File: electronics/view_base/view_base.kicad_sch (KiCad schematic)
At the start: 258 parts, among them J1 USB_C_Receptacle_USB2.0, J2 A, J3 B, J4 LCD, J5 59453-081110EDHLF, J6 BLDC, J7 SM04B-SRSS-TB(LF)(SN), J8 SM04B-SRSS-TB(LF)(SN), J9 SM04B-SRSS-TB(LF)(SN), Q1 MMBT4403, Q2 BSS138, Q3 BSS138, SW1 RST, SW2 Boot, U1 SN74LV1T34DBV, U10 LP5907MFX-2.8, U11 ESP32-S3-WROOM-1U-N16R8, U2 MT6701-CT, U3 VEML7700, U4 AMS1117-3.3, U5 USBLC6-2SC6, U6 HX711, U8 TMC6300, U9 VL53L0CXV0DH_1

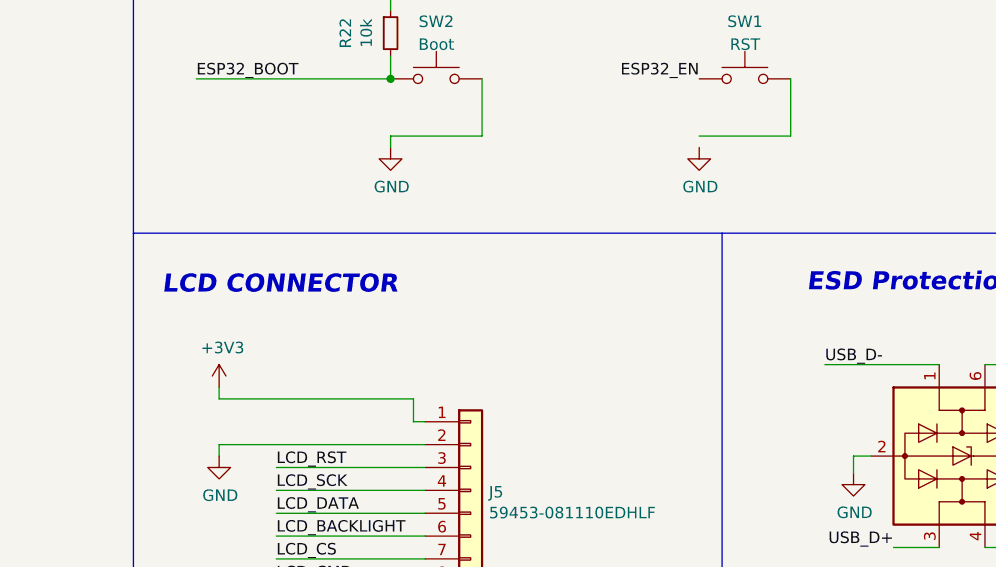
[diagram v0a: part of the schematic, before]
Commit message: Check github action for detect diff in the sch file
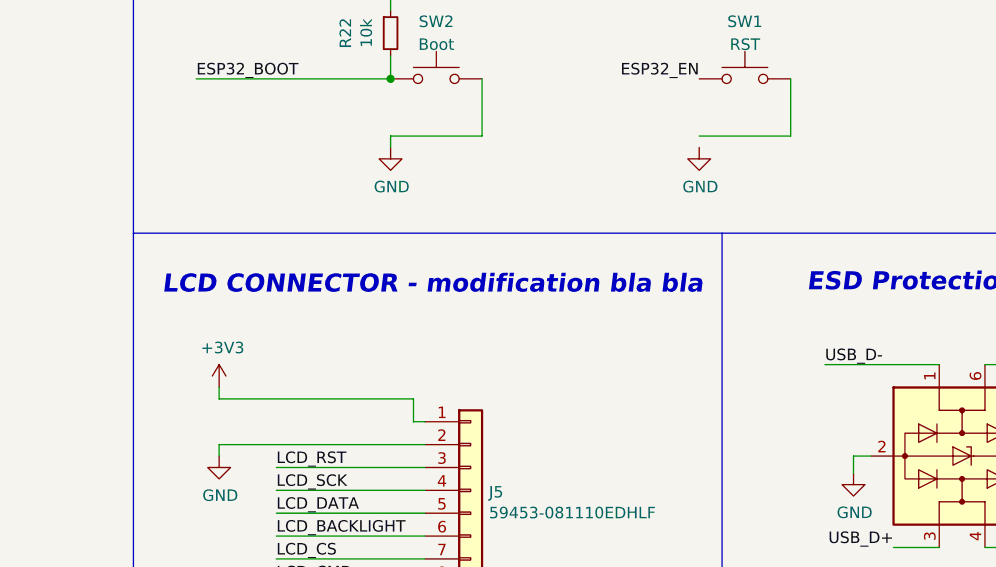
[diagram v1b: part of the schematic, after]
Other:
- note added: "LCD CONNECTOR - modification bla bla"
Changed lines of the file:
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@@
 		)
 	)
-	(text "LCD CONNECTOR"
+	(text "LCD CONNECTOR - modification bla bla"
 		(exclude_from_sim no)
 		(at 307.975 194.31 0)
